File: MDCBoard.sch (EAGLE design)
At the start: 202 parts, among them J1 JUMPER-SOLDER, J10 USB-C-RECEPTACLE-KOREANHRO, J2 JUMPER-SOLDER, J3 JUMPER-SOLDER, J4 JUMPER-SOLDER, J5 JST-SM02B-SRSS-TB, J6 JUMPER-SOLDER, J7 JUMPER-SOLDER, J8 JUMPER-SOLDER, J9 MICROSD-SOCKET, Q1 PMOS-NEXPERIA-SOT1220, Q2 PMOS-NEXPERIA-SOT1220, Q3 PMOS-NEXPERIA-SOT1220, Q4 DIODESINC-DMG2305UX, Q5 DIODESINC-DMG2305UX, Q6 DIODESINC-DMG2305UX, Q7 DIODESINC-DMG2305UX, Q8 DIODESINC-DMG2305UX, SW1 TACTILE-SWITCH, U1 TI-TPS2116, U10 TI-TPS22919DCK, U11 TI-TPS22919DCK, U12 TI-TPS22919DCK, U13 TI-TPS22919DCK, U14 TI-MSP430FR2433IRGE, U15 TI-TXB0102, U16 PANASONIC-EKMB110711X, U17 LATTICE-ICE40HX4K-BG121, U18 WINBOND-W25Q40EW, U19 NEXPERIA-74LVC1G98-OR-INV-INP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, U2 DIODESINC-AP7350, U20 NEXPERIA-74LVC1G98-BUFFER, U21 ON-AR0330CS1C12SPKA0, U22 ALLIANCE-AS4C8M16MSA-6BIN, U23 NEXPERIA-74LVC1G98-INVERTER, U24 STM-STM32F730, U25 DIODESINC-DT1446-04V-7, U3 NEXPERIA-74LVC1G98-NOR, U4 MICROCHIP-MCP7383X, U5 NEXPERIA-74LVC1G98-INVERTER, U6 EATON-STN101, U7 TI-TPS62A01, U8 TI-TPS62A01, U9 TI-TPS62A01, X1 EPSON-FC-135, X2 SITIME-SIT8021, X3 SITIME-SIT8021

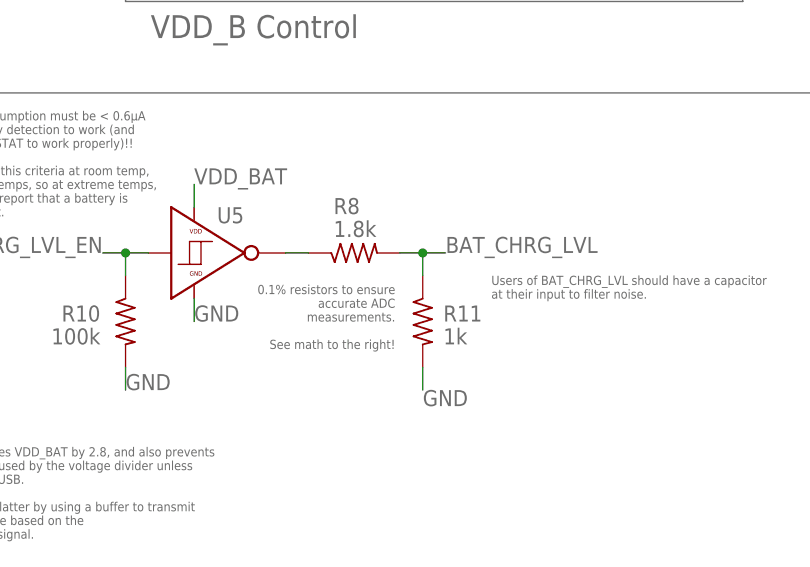
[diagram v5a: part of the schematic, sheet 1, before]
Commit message: Switch battery voltage divider dynamic range to [0,3.3]V
Now uses 1k-3k resistors
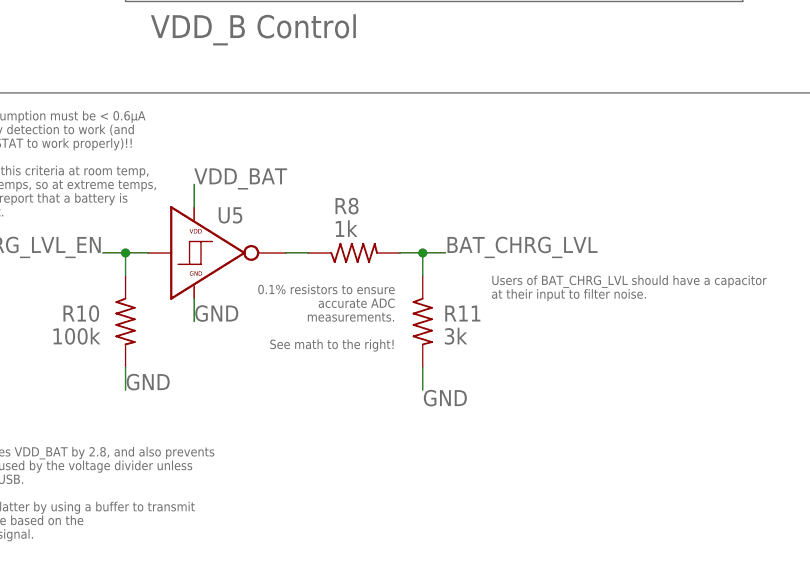
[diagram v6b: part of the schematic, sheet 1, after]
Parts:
- R11: value 1k -> 3k; PN RT0402BRD071KL -> RT0402BRD073KL
- R8: value 1.8k -> 1k; PN RT0402BRE071K8L -> RT0402BRD071KL
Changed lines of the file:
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@@
 <attribute name="PN" value="74LVC1G98GW,125"/>
 </part>
-<part name="R11" library="EagleLibrary" deviceset="RESISTOR" device="0402" value="1k">
+<part name="R11" library="EagleLibrary" deviceset="RESISTOR" device="0402" value="3k">
+<attribute name="MFG" value="Yageo"/>
+<attribute name="PN" value="RT0402BRD073KL"/>
+</part>
+<part name="R8" library="EagleLibrary" deviceset="RESISTOR" device="0402" value="1k">
 <attribute name="MFG" value="Yageo"/>
 <attribute name="PN" value="RT0402BRD071KL"/>
 </part>
-<part name="R8" library="EagleLibrary" deviceset="RESISTOR" device="0402" value="1.8k">
-<attribute name="MFG" value="Yageo"/>
-<attribute name="PN" value="RT0402BRE071K8L"/>
-</part>
 <part name="R6" library="EagleLibrary" deviceset="RESISTOR" device="0402" value="365k">

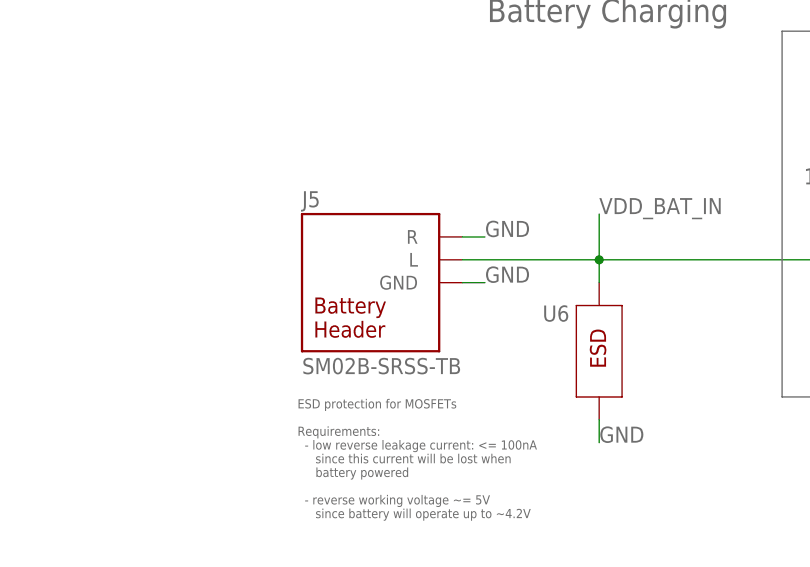
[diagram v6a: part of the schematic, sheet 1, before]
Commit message: Replace battery connector with Molex 781710002, still need to layout
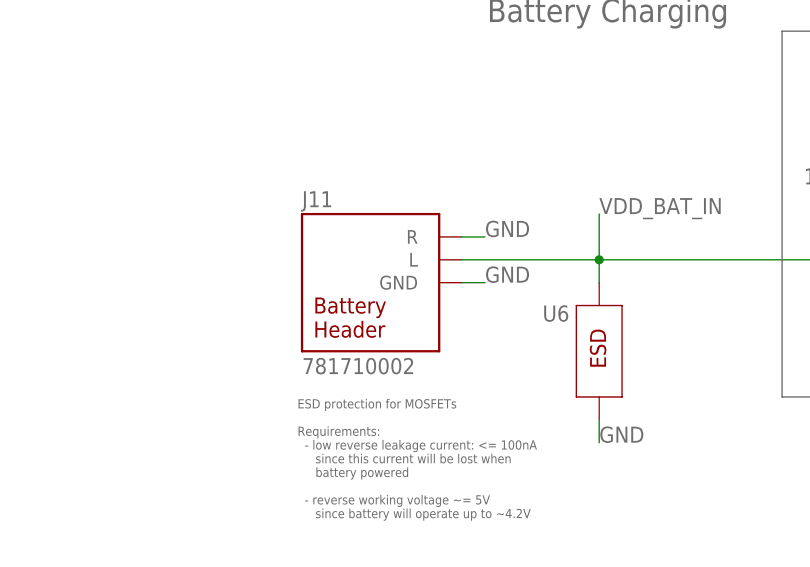
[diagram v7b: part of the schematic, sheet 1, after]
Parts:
- removed J5: JST-SM02B-SRSS-TB, EagleLibrary:JST-SM02B-SRSS-TB
- added J11: BATTERY-HEADER-MOLEX-781710002, EagleLibrary:BATTERY-HEADER-MOLEX-781710002
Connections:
- net GND: now also J11.GND, J11.R; no longer J5.GND, J5.R
- net VDD_BAT_IN: now also J11.L; no longer J5.L
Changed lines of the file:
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@@
 <attribute name="PN" value="STN101050B101"/>
 </part>
-<part name="J5" library="EagleLibrary" deviceset="JST-SM02B-SRSS-TB" device=""/>
 <part name="J10" library="EagleLibrary" deviceset="USB-C-RECEPTACLE" device="-KOREANHRO"/>
 <part name="R45" library="EagleLibrary" deviceset="RESISTOR" device="0402" value="5.1k">
@@
 <attribute name="PN" value="RC0402JR-0710KL"/>
 </part>
+<part name="J11" library="EagleLibrary" deviceset="BATTERY-HEADER" device="-MOLEX-781710002"/>
 </parts>
 <sheets>
@@
 <attribute name="PN" x="154.94" y="345.44" size="1.778" layer="96" rot="MR270" display="off"/>
 </instance>
-<instance part="J5" gate="G$1" x="124.46" y="355.6" smashed="yes">
-<attribute name="PN" x="124.46" y="337.82" size="1.778" layer="95"/>
-<attribute name="NAME" x="124.46" y="358.14" size="1.778" layer="95" align="top-left"/>
-</instance>
 <instance part="J4" gate="G$1" x="226.06" y="383.54" smashed="yes" rot="R270">
 <attribute name="NAME" x="228.6" y="384.81" size="1.778" layer="95" rot="R270" align="top-left"/>
@@
 <attribute name="MFG" x="259.08" y="447.04" size="1.778" layer="96" rot="R90" display="off"/>
 <attribute name="PN" x="259.08" y="447.04" size="1.778" layer="96" rot="R90" display="off"/>
+</instance>
+<instance part="J11" gate="G$1" x="124.46" y="355.6" smashed="yes">
+<attribute name="PN" x="124.46" y="337.82" size="1.778" layer="95"/>
+<attribute name="NAME" x="124.46" y="358.14" size="1.778" layer="95" align="top-left"/>
 </instance>
 </instances>
@@
 </segment>
 <segment>
-<pinref part="J5" gate="G$1" pin="GND"/>
 <wire x1="142.24" y1="347.98" x2="144.78" y2="347.98" width="0.1524" layer="91"/>
 <label x="144.78" y="347.98" size="1.778" layer="95"/>
-</segment>
-<segment>
-<pinref part="J5" gate="G$1" pin="R"/>
+<pinref part="J11" gate="G$1" pin="GND"/>
+</segment>
+<segment>
 <wire x1="142.24" y1="353.06" x2="144.78" y2="353.06" width="0.1524" layer="91"/>
 <label x="144.78" y="353.06" size="1.778" layer="95"/>
+<pinref part="J11" gate="G$1" pin="R"/>
 </segment>
 <segment>
@@
 <wire x1="157.48" y1="347.98" x2="157.48" y2="350.52" width="0.1524" layer="91"/>
 <junction x="157.48" y="350.52"/>
-<pinref part="J5" gate="G$1" pin="L"/>
 <wire x1="157.48" y1="350.52" x2="157.48" y2="355.6" width="0.1524" layer="91"/>
 <label x="157.48" y="355.6" size="1.778" layer="95"/>
-</segment>
-</net>
+<pinref part="J11" gate="G$1" pin="L"/>
+</segment>
+</net>

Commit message: Update part number of other 3k resistor to use the .1% version
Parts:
- R44: PN AC0402FR-073KL -> RT0402BRD073KL
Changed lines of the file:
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@@
 <part name="R44" library="EagleLibrary" deviceset="RESISTOR" device="0402" value="3k">
 <attribute name="MFG" value="Yageo"/>
-<attribute name="PN" value="AC0402FR-073KL"/>
+<attribute name="PN" value="RT0402BRD073KL"/>
 </part>
 <part name="C66" library="EagleLibrary" deviceset="CAPACITOR" device="0402" value="100n">
